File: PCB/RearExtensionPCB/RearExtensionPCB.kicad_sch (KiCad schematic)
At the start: 3 parts, among them J1 Conn_01x10, SW1 RotaryEncoder_Switch, U1 ER_OLEDM0.91_1x-I2C

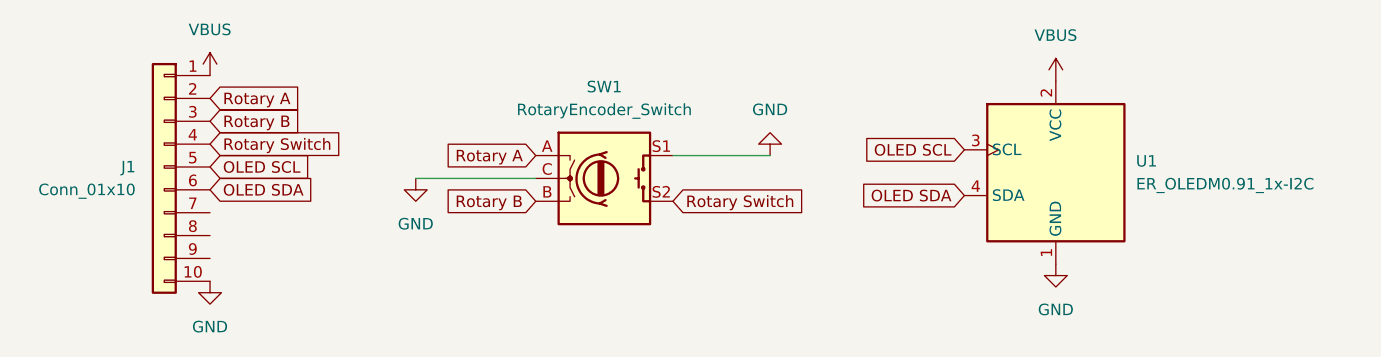
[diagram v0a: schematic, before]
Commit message: Finished Rear Extention and added 3D Models
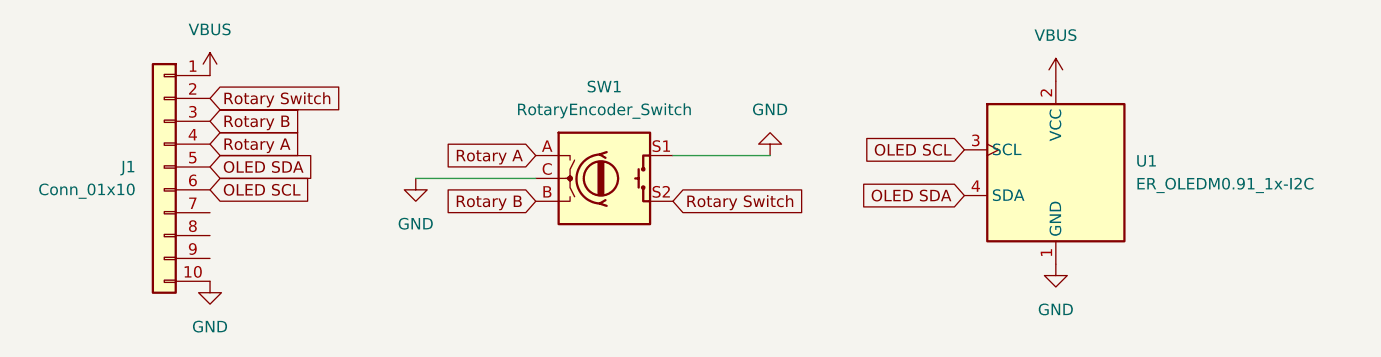
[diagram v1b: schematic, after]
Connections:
- net OLED SCL: now also J1.6 (Pin_6); no longer J1.5 (Pin_5)
- net OLED SDA: now also J1.5 (Pin_5); no longer J1.6 (Pin_6)
- net Rotary A: now also J1.4 (Pin_4); no longer J1.2 (Pin_2)
- net Rotary Switch: now also J1.2 (Pin_2); no longer J1.4 (Pin_4)
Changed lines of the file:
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@@
 	(global_label "OLED SDA"
 		(shape input)
-		(at 108.585 99.06 0)
+		(at 108.585 96.52 0)
 		(fields_autoplaced yes)
 		(effects
@@
 		)
 		(property "Intersheetrefs" "${INTERSHEET_REFS}"
-			(at 120.8835 99.06 0)
+			(at 120.8835 96.52 0)
 			(hide yes)
 			(show_name no)
@@
 	(global_label "Rotary Switch"
 		(shape input)
-		(at 108.585 93.98 0)
+		(at 108.585 88.9 0)
 		(fields_autoplaced yes)
 		(effects
@@
 		)
 		(property "Intersheetrefs" "${INTERSHEET_REFS}"
-			(at 124.6934 93.98 0)
+			(at 124.6934 88.9 0)
 			(hide yes)
 			(show_name no)
@@
 	(global_label "OLED SCL"
 		(shape input)
-		(at 108.585 96.52 0)
+		(at 108.585 99.06 0)
 		(fields_autoplaced yes)
 		(effects
@@
 		)
 		(property "Intersheetrefs" "${INTERSHEET_REFS}"
-			(at 120.823 96.52 0)
+			(at 120.823 99.06 0)
 			(hide yes)
 			(show_name no)
@@
 	(global_label "Rotary A"
 		(shape input)
-		(at 108.585 88.9 0)
+		(at 108.585 93.98 0)
 		(fields_autoplaced yes)
 		(effects
@@
 		)
 		(property "Intersheetrefs" "${INTERSHEET_REFS}"
-			(at 119.6739 88.9 0)
+			(at 119.6739 93.98 0)
 			(hide yes)
 			(show_name no)
